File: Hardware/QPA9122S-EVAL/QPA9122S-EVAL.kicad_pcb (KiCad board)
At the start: 2 copper layers, 58.5 x 32.9 mm, 20 parts, among them IC1 QPA9122TR7, J1 Conn_Coaxial, J2 Conn_Coaxial, J3 Conn_01x02_Pin, J4 Conn_01x02_Pin, J5 Conn_01x02_Pin, J6 Conn_Coaxial, J7 Conn_Coaxial

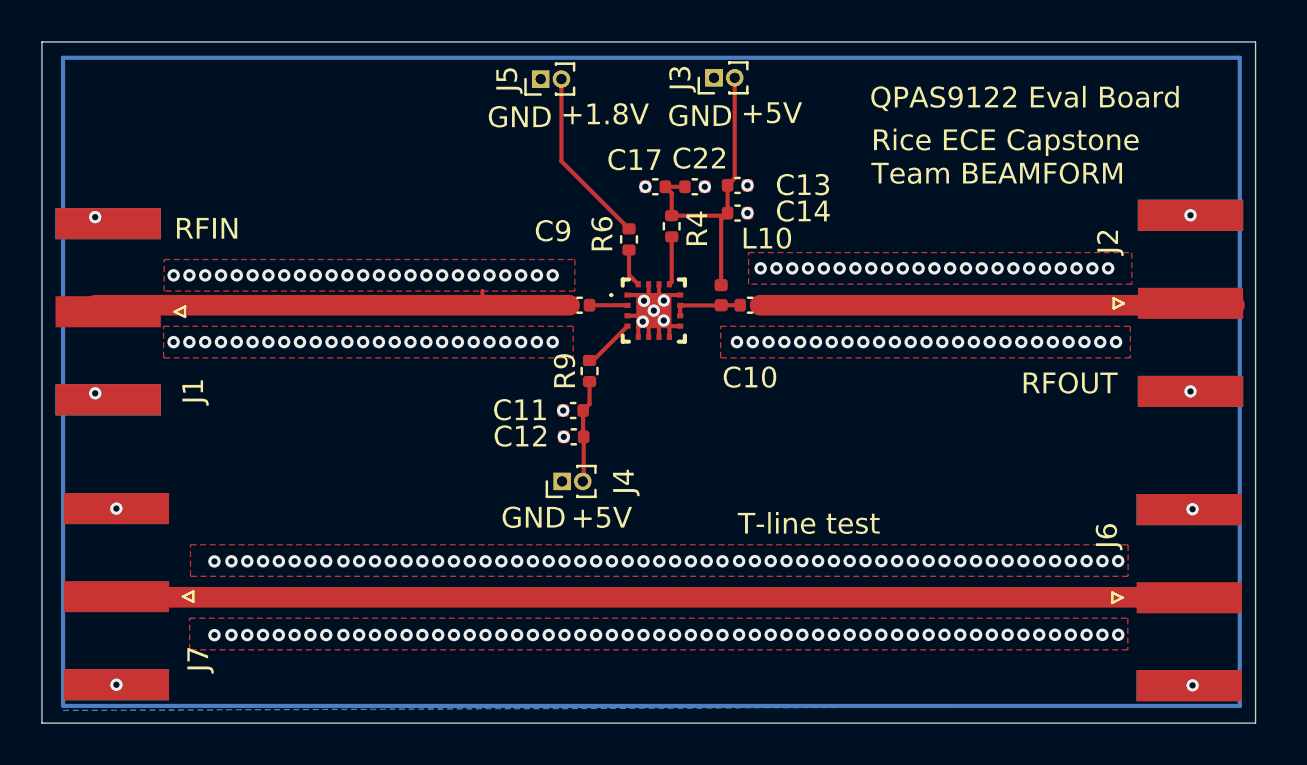
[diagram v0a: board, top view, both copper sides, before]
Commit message: T-line tuning
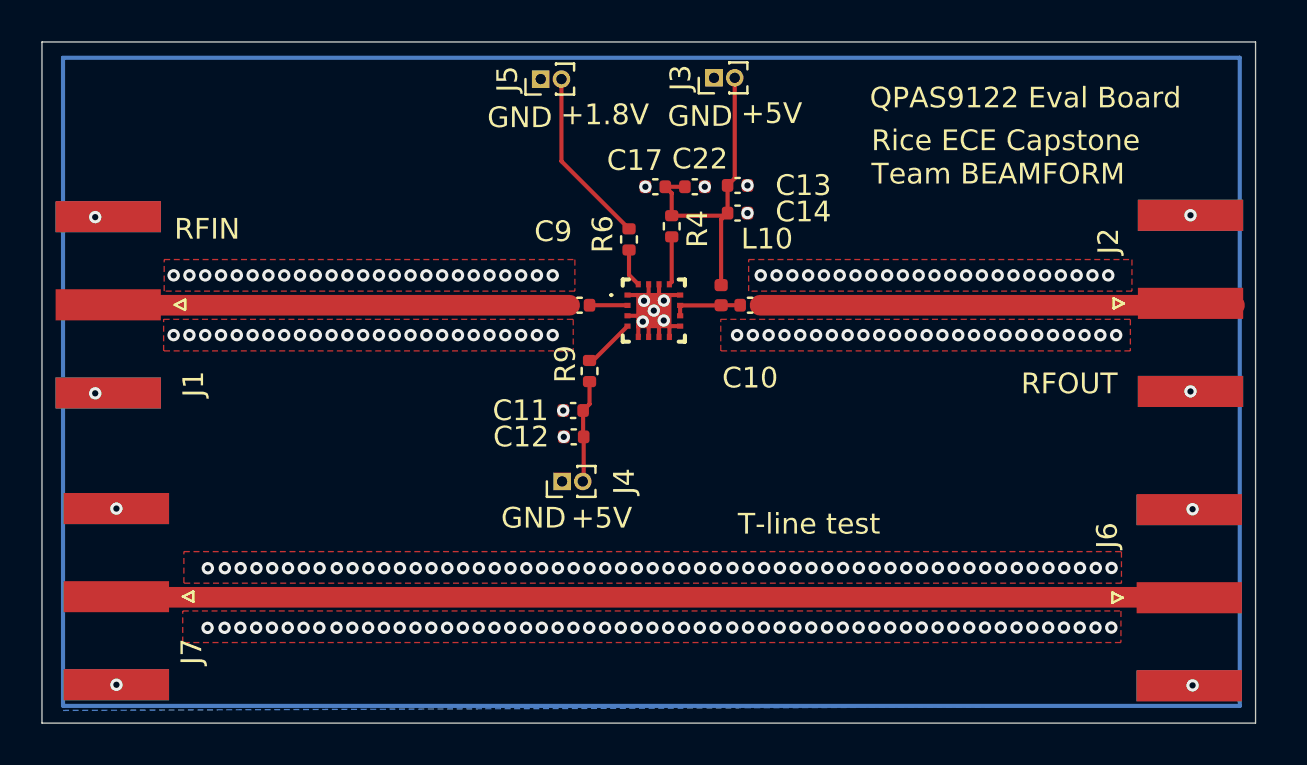
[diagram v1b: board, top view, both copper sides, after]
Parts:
- moved J1 0.34 mm to (93.0, 94.0)

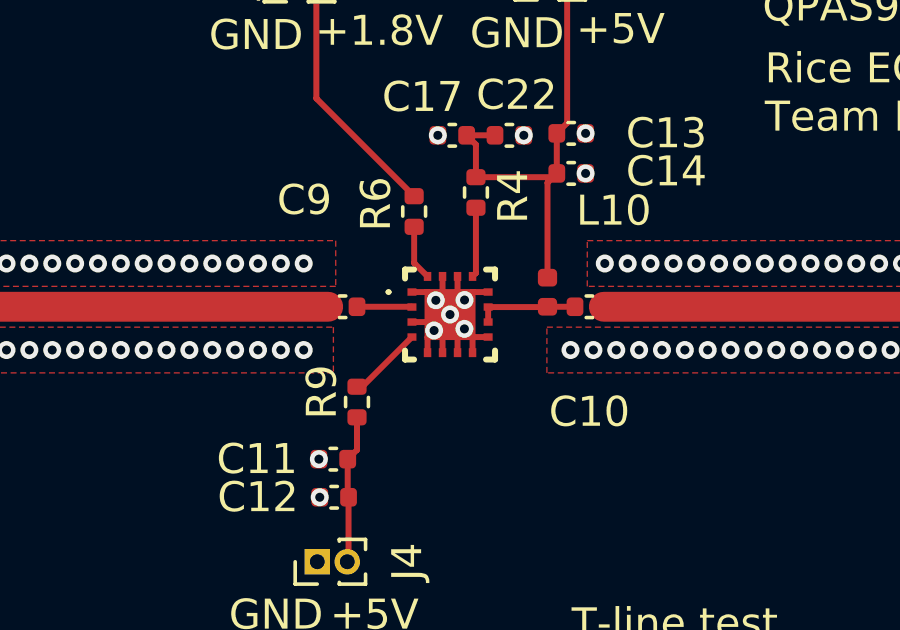
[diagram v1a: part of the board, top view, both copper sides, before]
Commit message: QPA via stitchinc
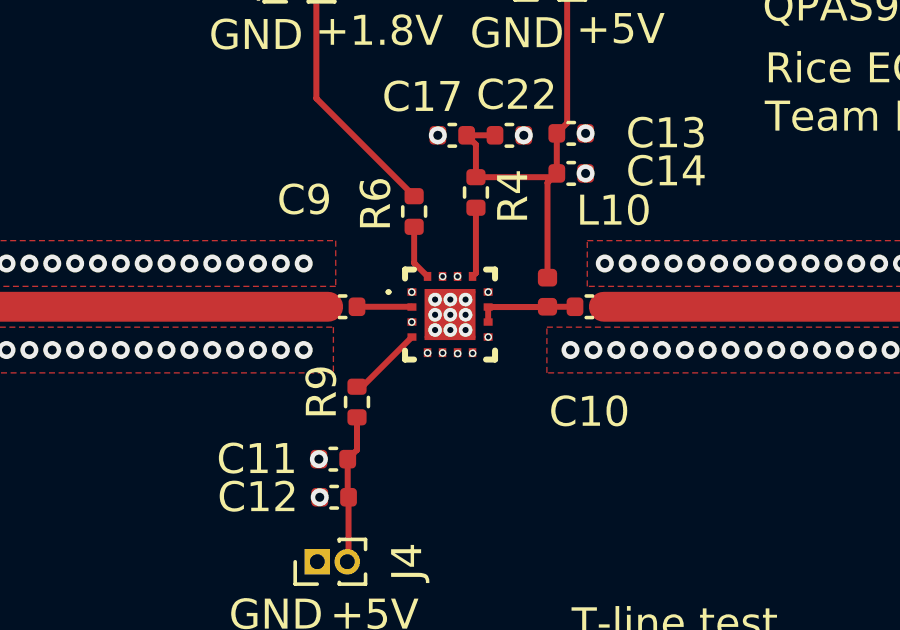
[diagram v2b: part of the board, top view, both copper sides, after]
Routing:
- net GND: track 13.4 -> 1.42 mm, vias 233 -> 247
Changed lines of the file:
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@@
 	)
 	(segment
-		(start 118.0367 93.489)
-		(end 118.5567 93.489)
-		(width 0.2)
-		(layer "F.Cu")
-		(net 5)
-	)
-	(segment
-		(start 119.5567 93.989)
+		(start 119.31545 94.24775)
 		(end 119.3067 94.239)
-		(width 0.2)
-		(layer "F.Cu")
-		(net 5)
-	)
-	(segment
-		(start 120.0567 95.509)
-		(end 120.0567 94.989)
-		(width 0.2)
-		(layer "F.Cu")
-		(net 5)
-	)
-	(segment
-		(start 119.0567 94.489)
-		(end 119.3067 94.239)
-		(width 0.2)
-		(layer "F.Cu")
-		(net 5)
-	)
-	(segment
-		(start 118.5567 95.509)
-		(end 118.5567 94.989)
 		(width 0.2)
 		(layer "F.Cu")
@@
 	)
 	(segment
-		(start 119.0567 95.509)
-		(end 119.0567 94.489)
-		(width 0.2)
-		(layer "F.Cu")
-		(net 5)
-	)
-	(segment
-		(start 118.77435 94.77135)
-		(end 119.3067 94.239)
-		(width 0.2)
-		(layer "F.Cu")
-		(net 5)
-	)
-	(segment
-		(start 119.79035 93.75535)
-		(end 119.3067 94.239)
-		(width 0.2)
-		(layer "F.Cu")
-		(net 5)
-	)
-	(segment
-		(start 119.5567 95.509)
-		(end 119.5567 94.489)
-		(width 0.2)
-		(layer "F.Cu")
-		(net 5)
-	)
-	(segment
-		(start 119.78535 94.71765)
-		(end 119.3067 94.239)
-		(width 0.2)
-		(layer "F.Cu")
-		(net 5)
-	)
-	(segment
 		(start 118.5567 94.989)
 		(end 118.77435 94.77135)
-		(width 0.2)
-		(layer "F.Cu")
-		(net 5)
-	)
-	(segment
-		(start 118.5567 93.489)
-		(end 118.83285 93.76515)
-		(width 0.2)
-		(layer "F.Cu")
-		(net 5)
-	)
-	(segment
-		(start 120.5767 94.989)
-		(end 120.0567 94.989)
-		(width 0.2)
-		(layer "F.Cu")
-		(net 5)
-	)
-	(segment
-		(start 119.0567 93.989)
-		(end 119.3067 94.239)
-		(width 0.2)
-		(layer "F.Cu")
-		(net 5)
-	)
-	(segment
-		(start 119.0567 92.969)
-		(end 119.0567 93.989)
 		(width 0.2)
 		(layer "F.Cu")
@@
 	)
 	(segment
-		(start 120.5767 93.489)
-		(end 120.0567 93.489)
+		(start 119.5567 94.489)
+		(end 119.31545 94.24775)
 		(width 0.2)
 		(layer "F.Cu")
 		(net 5)
 	)
-	(segment
-		(start 118.83285 93.76515)
-		(end 119.3067 94.239)
-		(width 0.2)
-		(layer "F.Cu")
-		(net 5)
-	)
-	(segment
-		(start 118.0367 94.489)
-		(end 119.0567 94.489)
-		(width 0.2)
-		(layer "F.Cu")
-		(net 5)
-	)
-	(segment
-		(start 119.5567 92.969)
-		(end 119.5567 93.989)
-		(width 0.2)
-		(layer "F.Cu")
-		(net 5)
-	)
-	(segment
-		(start 119.5567 94.489)
-		(end 119.3067 94.239)
-		(width 0.2)
-		(layer "F.Cu")
-		(net 5)
-	)
 	(via
 		(at 135.29433 106.654)
@@
 	)
 	(via
+		(at 119.56 95.54)
+		(size 0.254)
+		(drill 0.1524)
+		(layers "F.Cu" "B.Cu")
+		(free yes)
+		(net 5)
+	)
+	(via
 		(at 134.370975 92.538)
 		(size 0.6)
@@
 	)
 	(via
-		(at 118.83285 93.76515)
-		(size 0.6)
-		(drill 0.3)
-		(layers "F.Cu" "B.Cu")
+		(at 119.06 92.97)
+		(size 0.254)
+		(drill 0.1524)
+		(layers "F.Cu" "B.Cu")
+		(free yes)
 		(net 5)
 	)
@@
 	)
 	(via
+		(at 119.31545 93.73975)
+		(size 0.4572)
+		(drill 0.2032)
+		(layers "F.Cu" "B.Cu")
+		(net 5)
+	)
+	(via
 		(at 105.522 109.54)
 		(size 0.6)
@@
 	)
 	(via
+		(at 118.56 95.52)
+		(size 0.254)
+		(drill 0.1524)
+		(layers "F.Cu" "B.Cu")
+		(free yes)
+		(net 5)
+	)
+	(via
+		(at 119.82345 93.73975)
+		(size 0.4572)
+		(drill 0.2032)
+		(layers "F.Cu" "B.Cu")
+		(net 5)
+	)
+	(via
 		(at 110.86833 106.664)
 		(size 0.6)
@@
 	)
 	(via
+		(at 118.03 94.49)
+		(size 0.254)
+		(drill 0.1524)
+		(layers "F.Cu" "B.Cu")
+		(free yes)
+		(net 5)
+	)
+	(via
 		(at 113.142 109.54)
 		(size 0.6)
@@
 	)
 	(via
+		(at 119.31545 94.24775)
+		(size 0.4572)
+		(drill 0.2032)
+		(layers "F.Cu" "B.Cu")
+		(net 5)
+	)
+	(via
 		(at 136.05633 106.654)
 		(size 0.6)
@@
 	)
 	(via
+		(at 120.58 94.99)
+		(size 0.254)
+		(drill 0.1524)
+		(layers "F.Cu" "B.Cu")
+		(free yes)
+		(net 5)
+	)
+	(via
 		(at 131.322975 92.538)
 		(size 0.6)
@@
 	)
 	(via
-		(at 119.78535 94.71765)
-		(size 0.6)
-		(drill 0.3)
-		(layers "F.Cu" "B.Cu")
-		(net 5)
-	)
-	(via
 		(at 120.77433 106.664)
 		(size 0.6)
@@
 	)
 	(via
+		(at 120.58 93.49)
+		(size 0.254)
+		(drill 0.1524)
+		(layers "F.Cu" "B.Cu")
+		(free yes)
+		(net 5)
+	)
+	(via
 		(at 130.942872 95.422)
 		(size 0.6)
@@
 	)
 	(via
+		(at 119.5567 92.969)
+		(size 0.254)
+		(drill 0.1524)
+		(layers "F.Cu" "B.Cu")
+		(free yes)
+		(net 5)
+	)
+	(via
 		(at 124.846872 95.422)
 		(size 0.6)
@@
 	)
 	(via
+		(at 118.80745 93.73975)
+		(size 0.4572)
+		(drill 0.2032)
+		(layers "F.Cu" "B.Cu")
+		(net 5)
+	)
+	(via
 		(at 92.3575 98.23)
 		(size 0.6)
@@
 	)
 	(via
+		(at 119.31545 94.75575)
+		(size 0.4572)
+		(drill 0.2032)
+		(layers "F.Cu" "B.Cu")
+		(net 5)
+	)
+	(via
 		(at 137.418975 92.538)
 		(size 0.6)
@@
 	)
 	(via
-		(at 119.3067 94.239)
-		(size 0.6)
-		(drill 0.3)
-		(layers "F.Cu" "B.Cu")
-		(net 5)
-	)
-	(via
 		(at 138.562872 95.422)
 		(size 0.6)
@@
 	)
 	(via
+		(at 119.82345 94.75575)
+		(size 0.4572)
+		(drill 0.2032)
+		(layers "F.Cu" "B.Cu")
+		(net 5)
+	)
+	(via
 		(at 127.662 109.53)
 		(size 0.6)
@@
 	)
 	(via
-		(at 118.77435 94.77135)
-		(size 0.6)
-		(drill 0.3)
-		(layers "F.Cu" "B.Cu")
-		(net 5)
-	)
-	(via
 		(at 109.856831 92.538)
 		(size 0.6)
@@
 	)
 	(via
+		(at 119.06 95.52)
+		(size 0.254)
+		(drill 0.1524)
+		(layers "F.Cu" "B.Cu")
+		(free yes)
+		(net 5)
+	)
+	(via
 		(at 139.854 109.53)
 		(size 0.6)
@@
 	)
 	(via
-		(at 119.79035 93.75535)
-		(size 0.6)
-		(drill 0.3)
-		(layers "F.Cu" "B.Cu")
-		(net 5)
-	)
-	(via
 		(at 111.380831 92.538)
 		(size 0.6)
@@
 	)
 	(via
+		(at 118.03 93.49)
+		(size 0.254)
+		(drill 0.1524)
+		(layers "F.Cu" "B.Cu")
+		(free yes)
+		(net 5)
+	)
+	(via
 		(at 134.52 109.53)
 		(size 0.6)
@@
 	)
 	(via
+		(at 118.80745 94.75575)
+		(size 0.4572)
+		(drill 0.2032)
+		(layers "F.Cu" "B.Cu")
+		(net 5)
+	)
+	(via
 		(at 104.01033 106.664)
 		(size 0.6)
@@
 	)
 	(via
+		(at 119.82345 94.24775)
+		(size 0.4572)
+		(drill 0.2032)
+		(layers "F.Cu" "B.Cu")
+		(net 5)
+	)
+	(via
 		(at 103.759914 95.422)
 		(size 0.6)
@@
 	)
 	(via
+		(at 120.06 95.53)
+		(size 0.254)
+		(drill 0.1524)
+		(layers "F.Cu" "B.Cu")
+		(free yes)
+		(net 5)
+	)
+	(via
 		(at 120.762 109.54)
 		(size 0.6)
@@
 		(net 5)
 	)
+	(via
+		(at 118.80745 94.24775)
+		(size 0.4572)
+		(drill 0.2032)
+		(layers "F.Cu" "B.Cu")
+		(net 5)
+	)

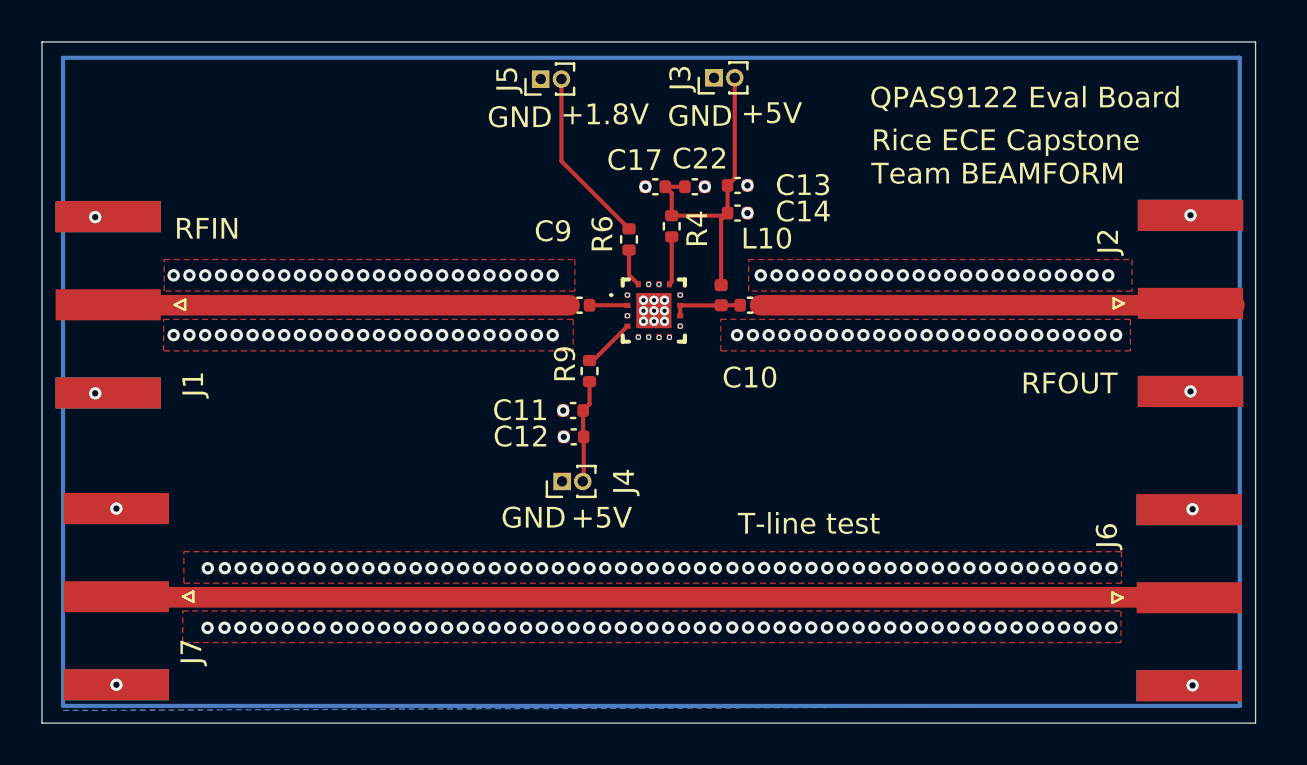
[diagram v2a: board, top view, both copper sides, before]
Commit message: amplifier SMA connections improvements
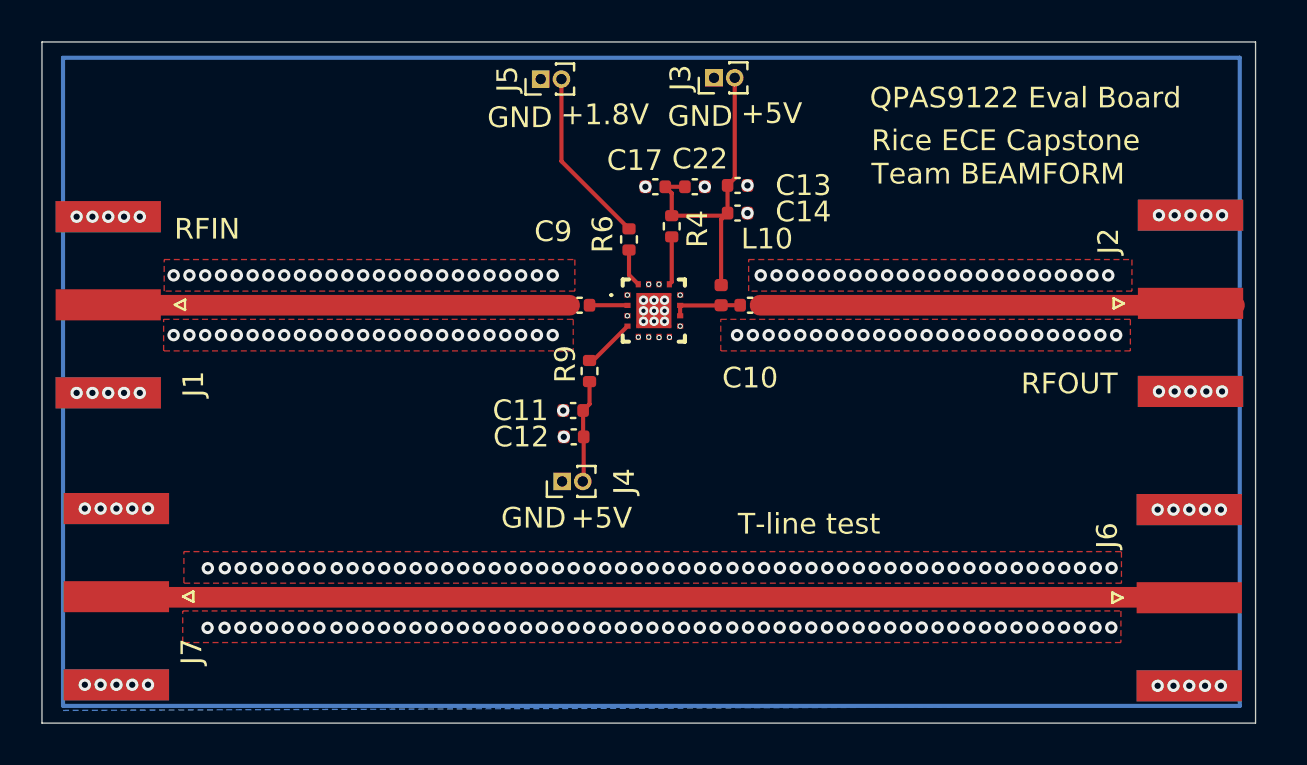
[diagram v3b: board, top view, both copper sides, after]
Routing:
- net GND: vias 247 -> 279

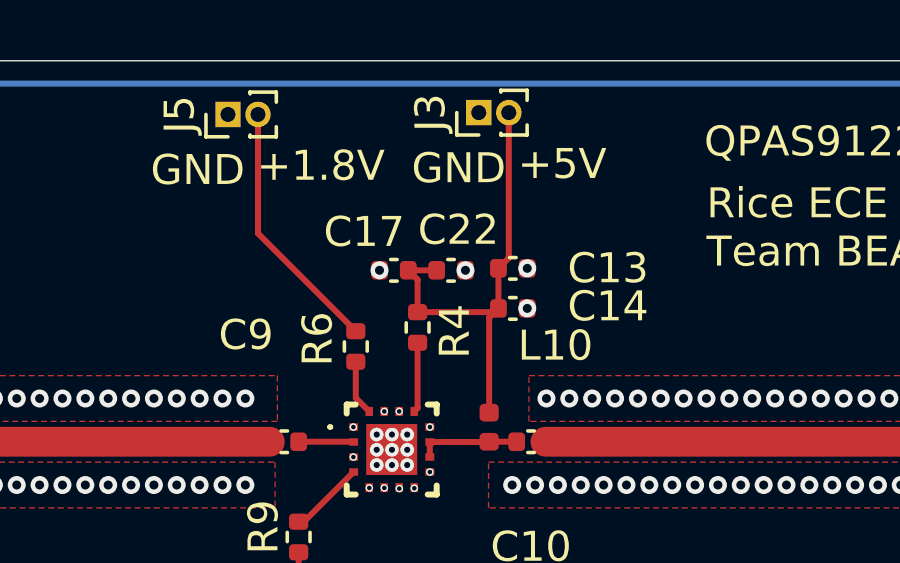
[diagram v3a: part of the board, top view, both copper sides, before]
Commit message: zero-ohm resistors/ferrite
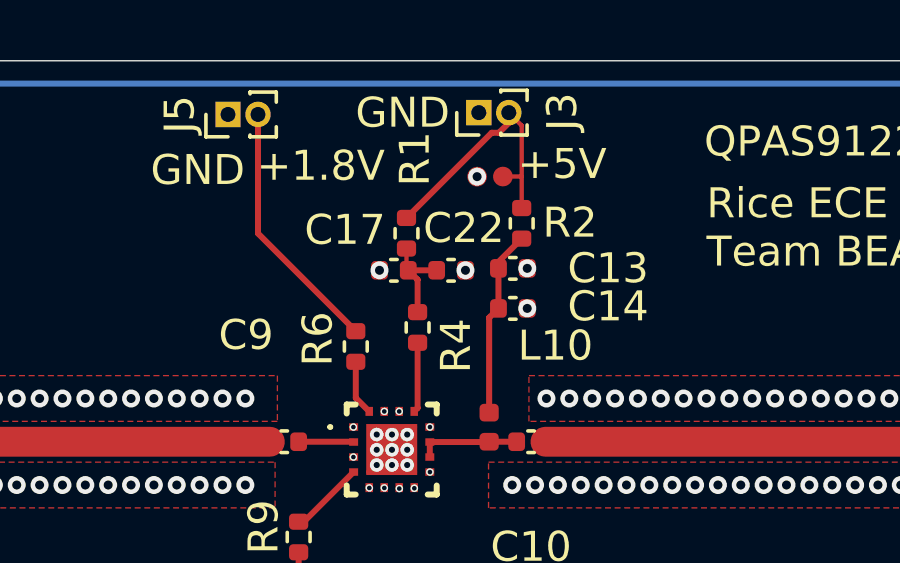
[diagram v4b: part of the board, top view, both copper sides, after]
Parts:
- added R1: 0, Resistor_SMD:R_0402_1005Metric, F.Cu at (119.8, 87.0)
- added R2: 0, Resistor_SMD:R_0402_1005Metric, F.Cu at (123.6, 86.7)
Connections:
- C13 pad 1: VCC -> Net-(C13-Pad1)
- C14 pad 1: VCC -> Net-(C13-Pad1)
- C17 pad 2: VCC -> Net-(C17-Pad2)
- C22 pad 1: VCC -> Net-(C17-Pad2)
- L10 pad 2: VCC -> Net-(C13-Pad1)
- R4 pad 1: VCC -> Net-(C17-Pad2)
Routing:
- net VCC: track 15.5 -> 9.02 mm
- net Net-(C13-Pad1): track 0.00 -> 6.43 mm
- net Net-(C17-Pad2): track 0.00 -> 3.22 mm
- net GND: vias 279 -> 280
